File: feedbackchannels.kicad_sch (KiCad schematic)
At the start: 95 parts, among them J18 FB CH1, J19 FB CH2, J20 FB CH3, J21 FB CH4, J22 VDET CH1, J23 VDET CH2, Q1 SI7220 NMOS, U21 TLP2366, U22 TLP2366, U23 TLP2366, U24 TLP2366, U25 TLP2366, U26 TLP2366, U27 TLV7031, U28 TLV7031, U29 LTC4367, U30 TLP2366, U31 TLP2366, U32 74LVC1G126, U33 AP64350, U34 PCA9534

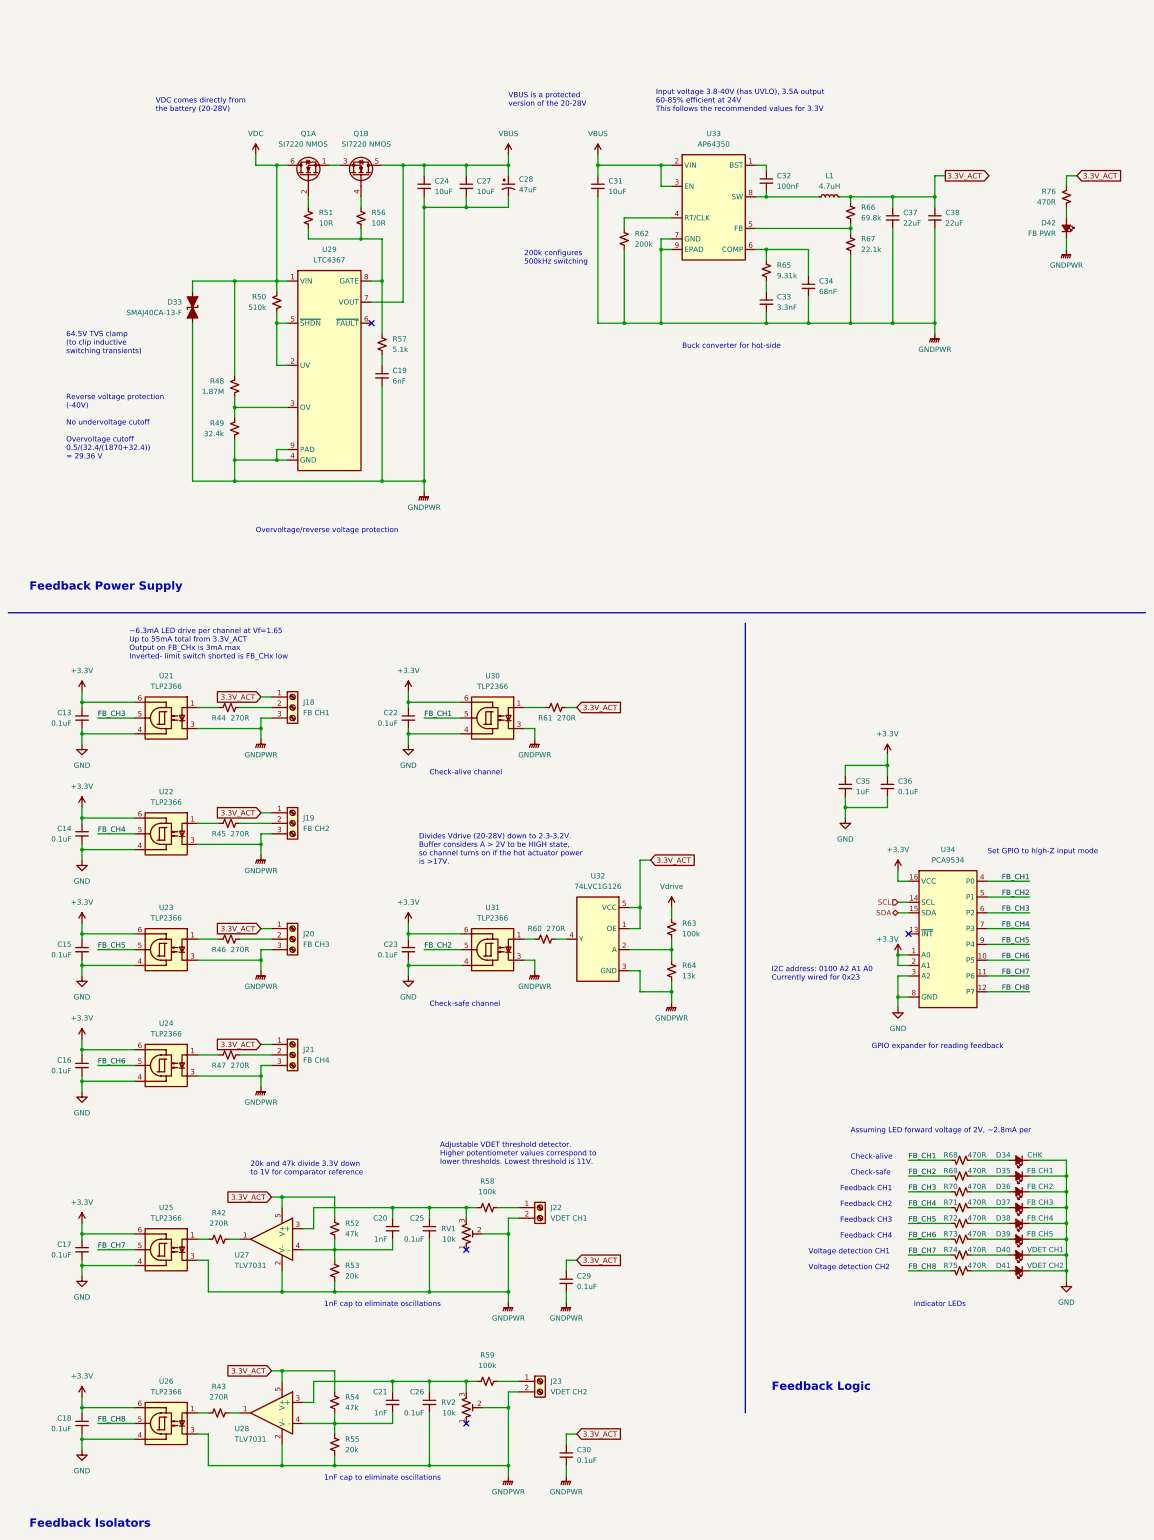
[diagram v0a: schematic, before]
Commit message: Added feedback indicator LED buffer and made changes to notes
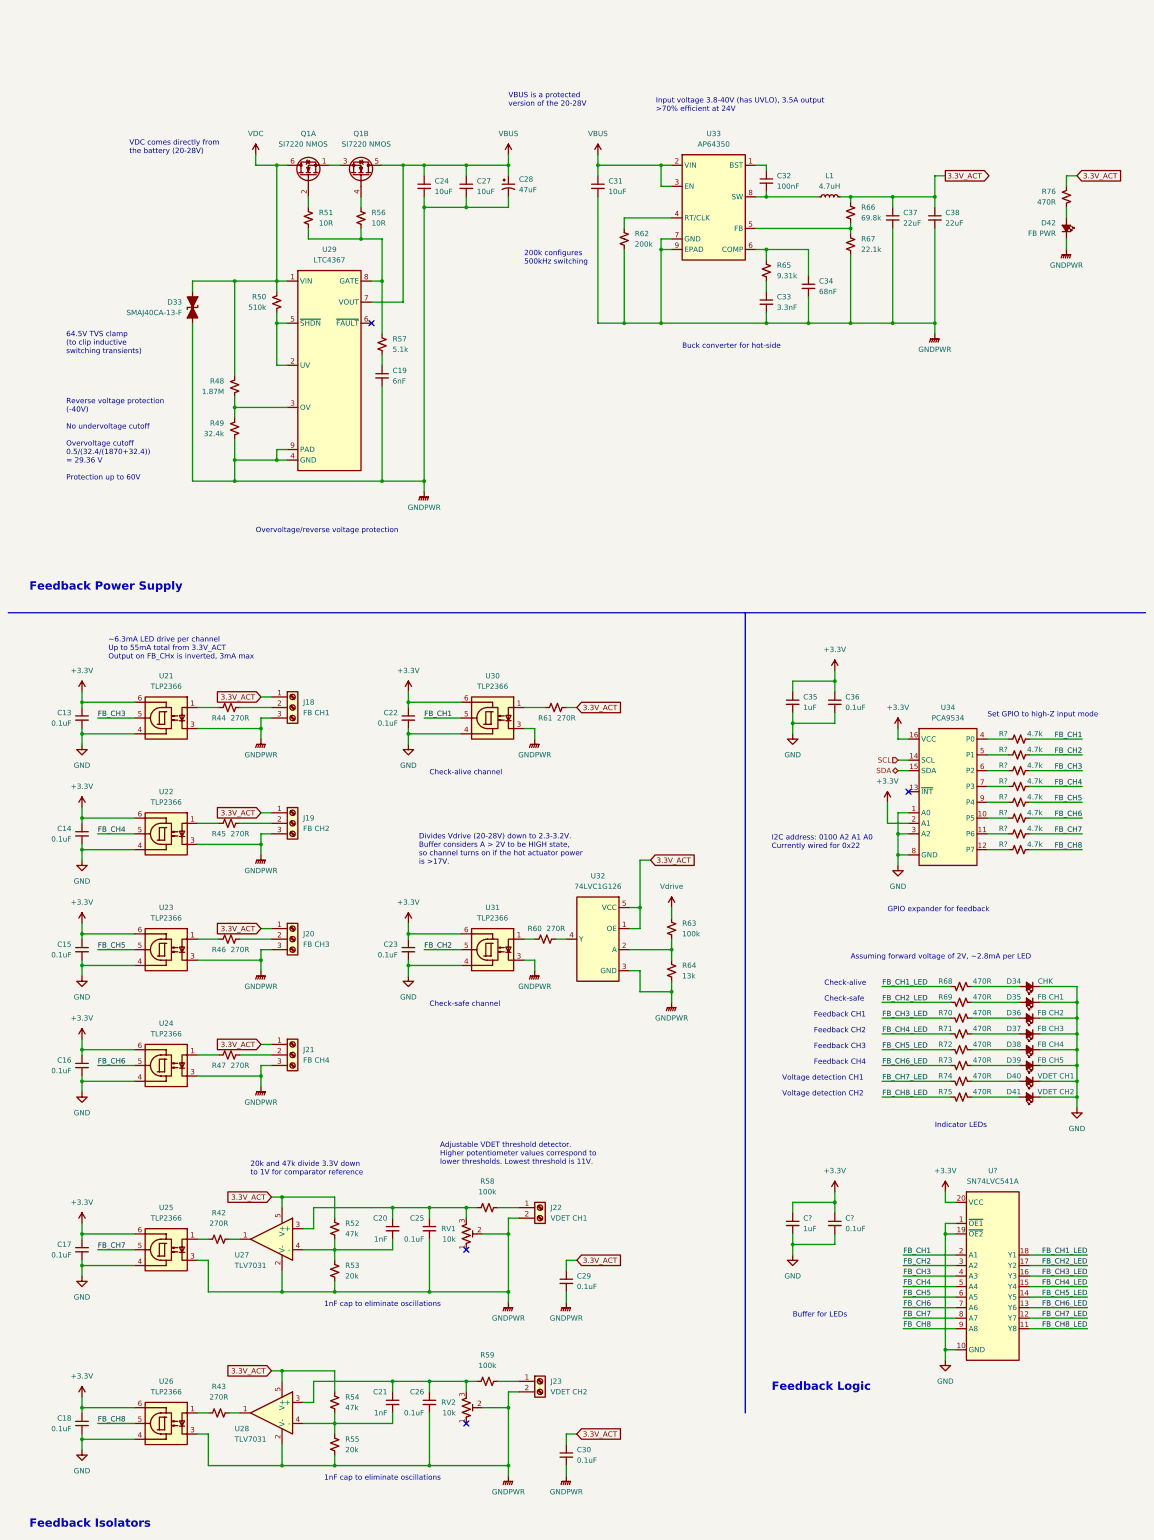
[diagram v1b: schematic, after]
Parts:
- added C?: 0.1uF, Capacitor_SMD:C_0603_1608Metric, symbol Device:C_Small
- added C?: 1uF, Capacitor_SMD:C_0603_1608Metric, symbol Device:C_Small
- added R? (x8): 4.7k, symbol Device:R_Small_US
- added U?: SN74LVC541A, Package_SO:TSSOP-20_4.4x6.5mm_P0.65mm, symbol actuation:SN74LVC541A
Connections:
- net +3.3V: now also C?.1, C?.1, U?.20 (VCC); no longer U34.1 (A0)
- net FB_CH1: now also R?.2, U?.2 (A1); no longer R68.1, U34.4 (P0)
- net FB_CH2: now also R?.2, U?.3 (A2); no longer R69.1, U34.5 (P1)
- net FB_CH3: now also R?.2, U?.4 (A3); no longer R70.1, U34.6 (P2)
- net FB_CH4: now also R?.2, U?.5 (A4); no longer R71.1, U34.7 (P3)
- net FB_CH5: now also R?.2, U?.6 (A5); no longer R72.1, U34.9 (P4)
- net FB_CH6: now also R?.2, U?.7 (A6); no longer R73.1, U34.10 (P5)
- net FB_CH7: now also R?.2, U?.8 (A7); no longer R74.1, U34.11 (P6)
- net FB_CH8: now also R?.2, U?.9 (A8); no longer R75.1, U34.12 (P7)
- net GND: now also U34.1 (A0), C?.2, C?.2, U?.1 (~{OE1}), U?.10 (GND), U?.19 (~{OE2})
- new net: R?.1, U34.10 (P5)
- new net: R?.1, U34.11 (P6)
- new net: R?.1, U34.12 (P7)
- new net: R?.1, U34.4 (P0)
- new net: R?.1, U34.5 (P1)
- new net: R?.1, U34.6 (P2)
- new net: R?.1, U34.7 (P3)
- new net: R?.1, U34.9 (P4)
- new net FB_CH1_LED: R68.1, U?.18 (Y1)
- new net FB_CH2_LED: R69.1, U?.17 (Y2)
- new net FB_CH3_LED: R70.1, U?.16 (Y3)
- new net FB_CH4_LED: R71.1, U?.15 (Y4)
- new net FB_CH5_LED: R72.1, U?.14 (Y5)
- new net FB_CH6_LED: R73.1, U?.13 (Y6)
- new net FB_CH7_LED: R74.1, U?.12 (Y7)
- new net FB_CH8_LED: R75.1, U?.11 (Y8)
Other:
- note added: "Assuming forward voltage of 2V, ~2.8mA per LED"
- note added: "Buffer for LEDs"
- note added: "GPIO expander for feedback"
- note added: "I2C address: 0100 A2 A1 A0 Currently wired for 0x22"
- note added: "Input voltage 3.8-40V (has UVLO), 3.5A output >70% efficient at 24V"
- note added: "Reverse voltage protection (-40V) No undervoltage cutoff Overvoltage cutoff 0.5/(32.4/(1870+32.4)) = 29.36 V Protection up to 60V"
- note added: "~6.3mA LED drive per channel Up to 55mA total from 3.3V_ACT Output on FB_CHx is inverted, 3mA max"
- note removed: "Assuming LED forward voltage of 2V, ~2.8mA per"
- note removed: "GPIO expander for reading feedback"
- note removed: "I2C address: 0100 A2 A1 A0 Currently wired for 0x23"
- note removed: "Input voltage 3.8-40V (has UVLO), 3.5A output 60-85% efficient at 24V This follows the recommended values for 3.3V"
- note removed: "Reverse voltage protection (-40V) No undervoltage cutoff Overvoltage cutoff 0.5/(32.4/(1870+32.4)) = 29.36 V"
- note removed: "~6.3mA LED drive per channel at Vf=1.65 Up to 55mA total from 3.3V_ACT Output on FB_CHx is 3mA max Inverted- limit switch shorted is FB_CHx low"
- moved on the sheet: C35, C36, D34, D35, D36, D37, D38, D39, D40, D41, R68, R69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

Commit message: Footprints, some part selection, external power outputs
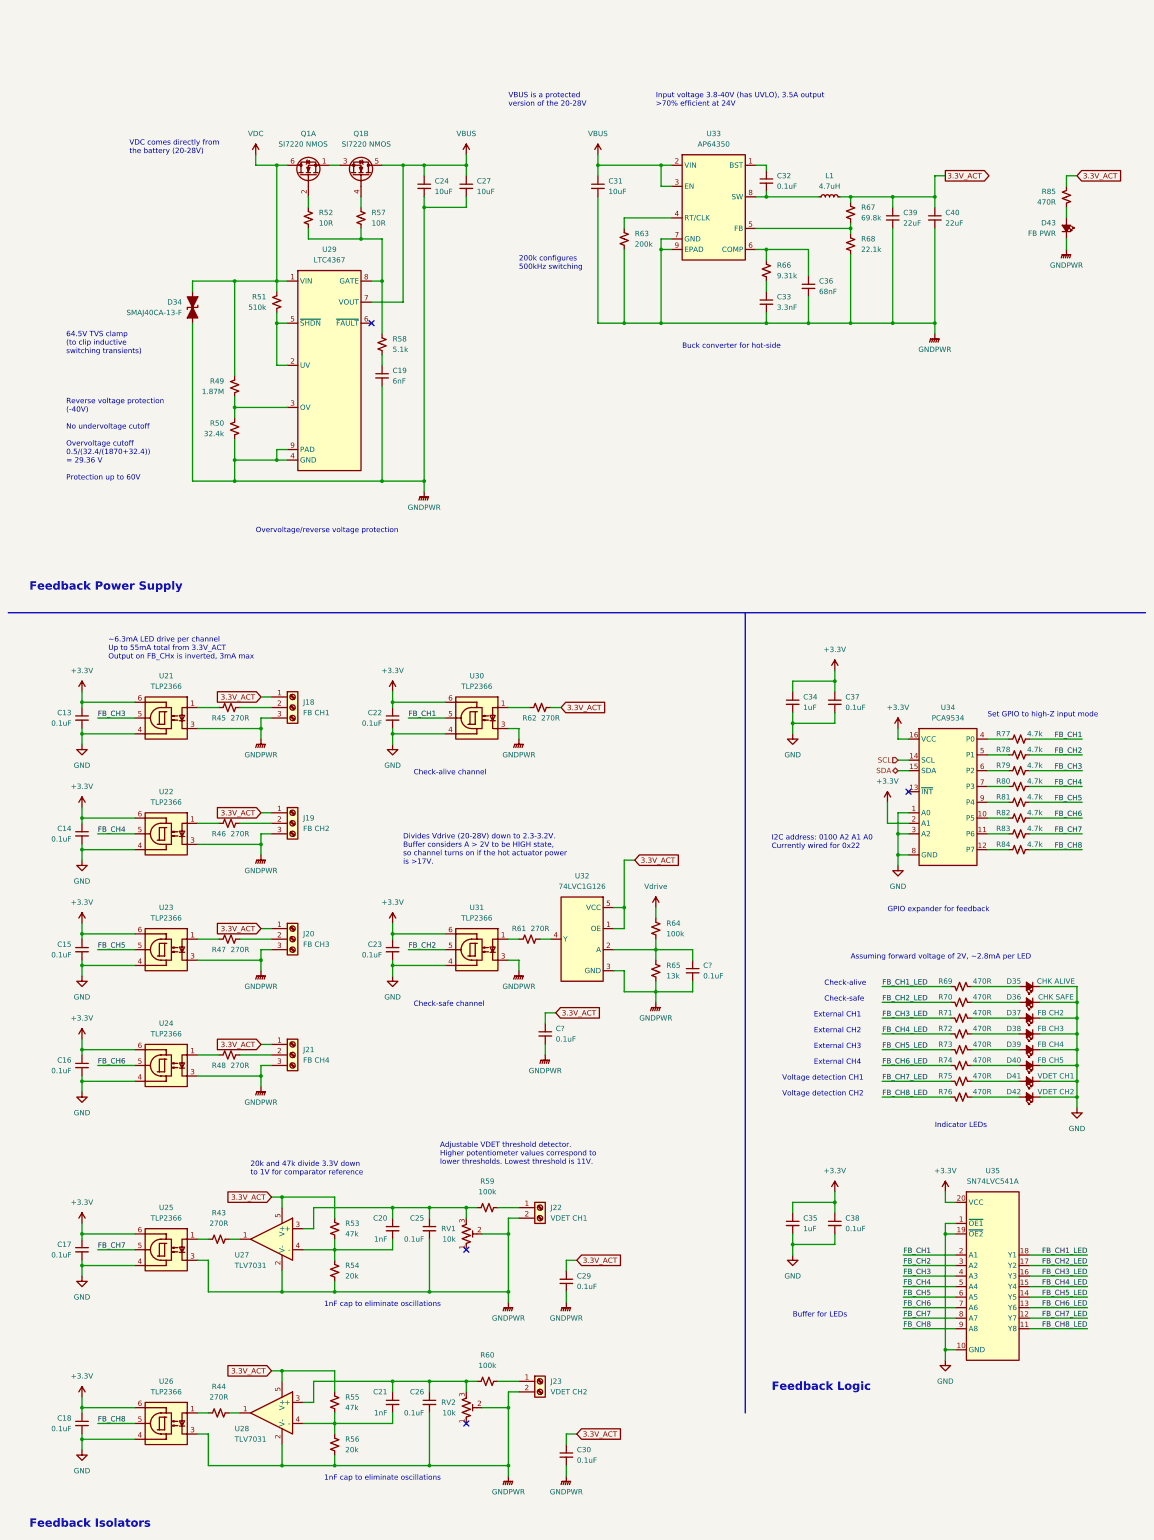
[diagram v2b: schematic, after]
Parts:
- removed C28: 47uF, Capacitor_SMD:CP_Elec_8x6.2, symbol Device:C_Polarized_Small_US
- added C? (x2): 0.1uF, Capacitor_SMD:C_0603_1608Metric, symbol Device:C_Small
- C20, C21, C25, C26, C29, C30, C33: footprint (none) -> Capacitor_SMD:C_0603_1608Metric
- C31: footprint (none) -> Capacitor_SMD:C_1206_3216Metric; MPN (none) -> CL31B106KBHNNNE
- C32: value 100nF -> 0.1uF; footprint (none) -> Capacitor_SMD:C_0603_1608Metric
- C36: renamed from C34; footprint (none) -> Capacitor_SMD:C_0603_1608Metric
- C39: renamed from C37; footprint (none) -> Capacitor_SMD:C_1206_3216Metric
- C40: renamed from C38; footprint (none) -> Capacitor_SMD:C_1206_3216Metric
- D35: renamed from D34; value CHK -> CHK ALIVE; footprint (none) -> LED_SMD:LED_0603_1608Metric
- D36: renamed from D35; value FB CH1 -> CHK SAFE; footprint (none) -> LED_SMD:LED_0603_1608Metric
- D37: renamed from D36; footprint (none) -> LED_SMD:LED_0603_1608Metric
- D38: renamed from D37; footprint (none) -> LED_SMD:LED_0603_1608Metric
- D39: renamed from D38; footprint (none) -> LED_SMD:LED_0603_1608Metric
- D40: renamed from D39; footprint (none) -> LED_SMD:LED_0603_1608Metric
- D41: renamed from D40; footprint (none) -> LED_SMD:LED_0603_1608Metric
- D42: renamed from D41; footprint (none) -> LED_SMD:LED_0603_1608Metric
- D43: renamed from D42; footprint (none) -> LED_SMD:LED_0603_1608Metric
- J18, J19, J20, J21: footprint (none) -> actuation:1751251
- J22, J23: footprint (none) -> actuation:1751248
- L1: footprint (none) -> Inductor_SMD:L_Vishay_IHLP-2020; MPN (none) -> IHLP2020CZER4R7M11
- R43: renamed from R42; footprint (none) -> Resistor_SMD:R_0603_1608Metric
- R44: renamed from R43; footprint (none) -> Resistor_SMD:R_0603_1608Metric
- R45: renamed from R44; footprint (none) -> Resistor_SMD:R_0603_1608Metric
- R46: renamed from R45; footprint (none) -> Resistor_SMD:R_0603_1608Metric
- R47: renamed from R46; footprint (none) -> Resistor_SMD:R_0603_1608Metric
- R48: renamed from R47; footprint (none) -> Resistor_SMD:R_0603_1608Metric
- R53: renamed from R52; footprint (none) -> Resistor_SMD:R_0603_1608Metric
- R54: renamed from R53; footprint (none) -> Resistor_SMD:R_0603_1608Metric
- R55: renamed from R54; footprint (none) -> Resistor_SMD:R_0603_1608Metric
- R56: renamed from R55; footprint (none) -> Resistor_SMD:R_0603_1608Metric
- R59: renamed from R58; footprint (none) -> Resistor_SMD:R_0603_1608Metric
- R60: renamed from R59; footprint (none) -> Resistor_SMD:R_0603_1608Metric
- R61: renamed from R60; footprint (none) -> Resistor_SMD:R_0603_1608Metric
- R62: renamed from R61; footprint (none) -> Resistor_SMD:R_0603_1608Metric
- R63: renamed from R62; footprint (none) -> Resistor_SMD:R_0603_1608Metric
- R64: renamed from R63; footprint (none) -> Resistor_SMD:R_0603_1608Metric
- R65: renamed from R64; footprint (none) -> Resistor_SMD:R_0603_1608Metric
- R66: renamed from R65; footprint (none) -> Resistor_SMD:R_0603_1608Metric
- R67: renamed from R66; footprint (none) -> Resistor_SMD:R_0603_1608Metric
- R68: renamed from R67; footprint (none) -> Resistor_SMD:R_0603_1608Metric
- R69: renamed from R68; footprint (none) -> Resistor_SMD:R_0603_1608Metric
- R70: renamed from R69; footprint (none) -> Resistor_SMD:R_0603_1608Metric
- R71: renamed from R70; footprint (none) -> Resistor_SMD:R_0603_1608Metric
- R72: renamed from R71; footprint (none) -> Resistor_SMD:R_0603_1608Metric
- R73: renamed from R72; footprint (none) -> Resistor_SMD:R_0603_1608Metric
- R74: renamed from R73; footprint (none) -> Resistor_SMD:R_0603_1608Metric
- R75: renamed from R74; footprint (none) -> Resistor_SMD:R_0603_1608Metric
- R76: renamed from R75; footprint (none) -> Resistor_SMD:R_0603_1608Metric
- R77, R78, R79, R80, R81, R82, R83, R84: renamed from R?; footprint (none) -> Resistor_SMD:R_0603_1608Metric
- R85: renamed from R76; footprint (none) -> Resistor_SMD:R_0603_1608Metric
- RV1, RV2: footprint (none) -> Resistor_SMD:R_0603_1608Metric
- gave numbers to parts that had none: 3
- renumbered C35 to C34, C36 to C37, D33 to D34, R48 to R49, R49 to R50, R50 to R51, R51 to R52, R56 to R57, R57 to R58
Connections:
- net 3.3V_ACT: now also C?.1
- net GNDPWR: now also C?.2, C?.2
- net at R64.2, R65.1, U32.2 (A): now also C?.1
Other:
- note added: "External CH1"
- note added: "External CH2"
- note added: "External CH3"
- note added: "External CH4"
- note removed: "Feedback CH1"
- note removed: "Feedback CH2"
- note removed: "Feedback CH3"
- note removed: "Feedback CH4"
- moved on the sheet: C22, C23, R61, R62, R64, R65, U30, U31, U32

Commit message: Schematic reorganization
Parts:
- removed C19: 6nF, Capacitor_SMD:C_0603_1608Metric, symbol Device:C_Small
- removed C24, C27, C31: 10uF, Capacitor_SMD:C_1206_3216Metric, symbol Device:C_Small
- removed C32: 0.1uF, Capacitor_SMD:C_0603_1608Metric, symbol Device:C_Small
- removed C33: 3.3nF, Capacitor_SMD:C_0603_1608Metric, symbol Device:C_Small
- removed C36: 68nF, Capacitor_SMD:C_0603_1608Metric, symbol Device:C_Small
- removed C39, C40: 22uF, Capacitor_SMD:C_1206_3216Metric, symbol Device:C_Small
- removed D34: SMAJ40CA-13-F, Diode_SMD:D_SMA, symbol Device:D_TVS_Filled
- removed D43: FB PWR, LED_SMD:LED_0603_1608Metric, symbol Device:LED_Small_Filled
- removed L1: 4.7uH, Inductor_SMD:L_Vishay_IHLP-2020, symbol Device:L_Small
- removed Q1: SI7220 NMOS, Package_SO:Vishay_PowerPAK_1212-8_Dual, symbol Device:Q_Dual_NMOS_S1G1S2G2D2D2D1D1
- removed R49: 1.87M, Resistor_SMD:R_0603_1608Metric, symbol Device:R_Small_US
- removed R50: 32.4k, Resistor_SMD:R_0603_1608Metric, symbol Device:R_Small_US
- removed R51: 510k, Resistor_SMD:R_0603_1608Metric, symbol Device:R_Small_US
- removed R52, R57: 10R, Resistor_SMD:R_0603_1608Metric, symbol Device:R_Small_US
- removed R58: 5.1k, Resistor_SMD:R_0603_1608Metric, symbol Device:R_Small_US
- removed R63: 200k, Resistor_SMD:R_0603_1608Metric, symbol Device:R_Small_US
- removed R66: 9.31k, Resistor_SMD:R_0603_1608Metric, symbol Device:R_Small_US
- removed R67: 69.8k, Resistor_SMD:R_0603_1608Metric, symbol Device:R_Small_US
- removed R68: 22.1k, Resistor_SMD:R_0603_1608Metric, symbol Device:R_Small_US
- removed R85: 470R, Resistor_SMD:R_0603_1608Metric, symbol Device:R_Small_US
- removed U29: LTC4367, Package_DFN_QFN:DFN-8-1EP_3x3mm_P0.5mm_EP1.65x2.38mm, symbol interface:LTC4367
- removed U33: AP64350, Package_SO:SOIC-8-1EP_3.9x4.9mm_P1.27mm_EP2.62x3.51mm, symbol actuation:AP64350
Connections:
- no-connect marks 4 -> 3
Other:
- note removed: "200k configures 500kHz switching"
- note removed: "64.5V TVS clamp (to clip inductive switching transients)"
- note removed: "Buck converter for hot-side"
- note removed: "Feedback Power Supply"
- note removed: "Input voltage 3.8-40V (has UVLO), 3.5A output >70% efficient at 24V"
- note removed: "Overvoltage/reverse voltage protection"
- note removed: "Reverse voltage protection (-40V) No undervoltage cutoff Overvoltage cutoff 0.5/(32.4/(1870+32.4)) = 29.36 V Protection up to 60V"
- note removed: "VBUS is a protected version of the 20-28V"
- note removed: "VDC comes directly from the battery (20-28V)"
- moved on the sheet: C13, C14, C15, C16, C17, C18, C20, C21, C22, C23, C25, C26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
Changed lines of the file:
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@@
 (kicad_sch (version 20211123) (generator eeschema)
-  (paper "User" 299.999 380.009)
+  (paper "User" 299.999 250.012)
